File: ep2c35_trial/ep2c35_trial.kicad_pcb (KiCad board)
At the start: 4 copper layers, 50.3 x 39 mm, 5 parts, among them U1 EP2C5F484

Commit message: EP2C35 trial. WIP.
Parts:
- added J1: Conn_02x21_Odd_Even, Connector_PinHeader_1.27mm:PinHeader_2x21_P1.27mm_Horizontal, F.Cu at (143.2, 101.7)
- added J2: Conn_02x21_Odd_Even, Connector_PinHeader_1.27mm:PinHeader_2x21_P1.27mm_Horizontal, F.Cu at (171.2, 101.7)
- added J3: 3M_8540-4500PL, logic_analyzer:3M_8540-4500PL, F.Cu at (111.5, 100.2)
- added R11: 100, Resistor_SMD:R_0402_1005Metric, B.Cu at (154.5, 83.0)
- added R12: 100, Resistor_SMD:R_0402_1005Metric, B.Cu at (154.5, 84.0)
- added R13: 100, Resistor_SMD:R_0402_1005Metric, B.Cu at (154.5, 85.0)
- added R14: 100, Resistor_SMD:R_0402_1005Metric, B.Cu at (154.5, 86.0)
- added R15: 100, Resistor_SMD:R_0402_1005Metric, B.Cu at (154.5, 87.0)
- added R16: 100, Resistor_SMD:R_0402_1005Metric, B.Cu at (154.5, 88.0)
- added R17: 100, Resistor_SMD:R_0402_1005Metric, B.Cu at (154.5, 89.0)
- added R18: 100, Resistor_SMD:R_0402_1005Metric, B.Cu at (154.5, 90.0)
- added R19: 100, Resistor_SMD:R_0402_1005Metric, B.Cu at (152.2, 90.2)
- added R20: 100, Resistor_SMD:R_0402_1005Metric, B.Cu at (154.5, 82.0)
- added R21: 100, Resistor_SMD:R_0402_1005Metric, B.Cu at (134.5, 90.0)
- added R22: 100, Resistor_SMD:R_0402_1005Metric, B.Cu at (134.5, 89.0)
- added R23: 100, Resistor_SMD:R_0402_1005Metric, B.Cu at (134.5, 88.0)
- added R24: 100, Resistor_SMD:R_0402_1005Metric, B.Cu at (134.5, 87.0)
- added R25: 100, Resistor_SMD:R_0402_1005Metric, B.Cu at (134.5, 86.0)
- added R26: 100, Resistor_SMD:R_0402_1005Metric, B.Cu at (134.5, 85.0)
- added R27: 100, Resistor_SMD:R_0402_1005Metric, B.Cu at (134.5, 84.0)
- added R28: 100, Resistor_SMD:R_0402_1005Metric, B.Cu at (134.5, 83.0)
- added R29: 100, Resistor_SMD:R_0402_1005Metric, B.Cu at (136.7, 90.2)
- added R30: 100, Resistor_SMD:R_0402_1005Metric, B.Cu at (134.5, 82.0)
- added U2: XC6SLX16-FTG256, Package_BGA:Xilinx_FTG256, F.Cu at (173.2, 69.6)
- added U3: FT600Q-B-T, logic_analyzer:QFN-56-1EP_7x7mm_P0.4mm_FT600Q, F.Cu at (144.4, 60.8)
- moved C1 0.05 mm to (149.0, 75.5)
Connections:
- U1 pad A10: unconnected-(U1-PadA10) -> /FT_WR_N
- U1 pad A11: unconnected-(U1-PadA11) -> /FT_OE_N
- U1 pad A2: +2V5 -> +3.3V
- U1 pad A21: +2V5 -> +3.3V
- U1 pad A3: unconnected-(U1-PadA3) -> /FT_DATA7
- U1 pad A4: unconnected-(U1-PadA4) -> /FT_DATA8
- U1 pad A5: unconnected-(U1-PadA5) -> /FT_DATA10
- U1 pad A6: unconnected-(U1-PadA6) -> /FT_DATA12
- U1 pad A7: unconnected-(U1-PadA7) -> /FT_DATA14
- U1 pad A8: unconnected-(U1-PadA8) -> /FT_BE0
- U1 pad A9: unconnected-(U1-PadA9) -> /FT_TXE_N
- U1 pad B1: +2V5 -> +3.3V
- U1 pad B10: unconnected-(U1-PadB10) -> /FT_RD_N
- U1 pad B11: unconnected-(U1-PadB11) -> /FT_RESET_N
- U1 pad B22: +2V5 -> +3.3V
- U1 pad B3: unconnected-(U1-PadB3) -> /FT_CLK
- U1 pad B4: unconnected-(U1-PadB4) -> /FT_DATA9
- U1 pad B5: unconnected-(U1-PadB5) -> /FT_DATA11
- U1 pad B6: unconnected-(U1-PadB6) -> /FT_DATA13
- U1 pad B7: unconnected-(U1-PadB7) -> /FT_DATA15
- U1 pad B8: unconnected-(U1-PadB8) -> /FT_BE1
- U1 pad B9: unconnected-(U1-PadB9) -> /FT_RXF_N
- U1 pad C1: unconnected-(U1-PadC1) -> /FT_DATA5
- U1 pad C10: unconnected-(U1-PadC10) -> /FT_GPIO1
- U1 pad C11: +2V5 -> +3.3V
- U1 pad C12: +2V5 -> +3.3V
- U1 pad C2: unconnected-(U1-PadC2) -> /FT_DATA6
- U1 pad C6: +2V5 -> +3.3V
- U1 pad C9: unconnected-(U1-PadC9) -> /FT_WAKEUP_N
- U1 pad D1: unconnected-(U1-PadD1) -> /FT_DATA3
- U1 pad D17: +2V5 -> +3.3V
- U1 pad D2: unconnected-(U1-PadD2) -> /FT_DATA4
- U1 pad D9: unconnected-(U1-PadD9) -> /FT_GPIO0
- U1 pad E1: unconnected-(U1-PadE1) -> /FT_DATA1
- U1 pad E10: +2V5 -> +3.3V
- U1 pad E13: +2V5 -> +3.3V
- U1 pad E2: unconnected-(U1-PadE2) -> /FT_DATA2
- U1 pad F2: unconnected-(U1-PadF2) -> /FT_DATA0
- U1 pad G14: +2V5 -> +3.3V
- U1 pad G19: +2V5 -> +3.3V
- U1 pad G9: +2V5 -> +3.3V
- U1 pad J16: +2V5 -> +3.3V
- U1 pad J7: +2V5 -> +3.3V
- U1 pad L20: +2V5 -> +3.3V
- U1 pad L3: +2V5 -> +3.3V
- U1 pad M1: unconnected-(U1-PadM1) -> /LVDS_RX_CLK0_P
- U1 pad M2: unconnected-(U1-PadM2) -> /LVDS_RX_CLK0_N
- U1 pad M21: unconnected-(U1-PadM21) -> /LVDS_RX_CLK1_N
- U1 pad M22: unconnected-(U1-PadM22) -> GNDD
- U1 pad M5: unconnected-(U1-PadM5) -> Net-(U1-PadM5)
- U1 pad M6: unconnected-(U1-PadM6) -> Net-(U1-PadM5)
- U1 pad M7: unconnected-(U1-PadM7) -> Net-(U1-PadM7)
- U1 pad M8: unconnected-(U1-PadM8) -> Net-(U1-PadM7)
- U1 pad N1: unconnected-(U1-PadN1) -> /LVDS_RX_DATA0_0_P
- U1 pad N2: unconnected-(U1-PadN2) -> /LVDS_RX_DATA0_0_N
- U1 pad N21: unconnected-(U1-PadN21) -> /LVDS_RX_DATA1_7_N
- U1 pad N22: unconnected-(U1-PadN22) -> /LVDS_RX_DATA1_7_P
- U1 pad N3: unconnected-(U1-PadN3) -> Net-(U1-PadN3)
- U1 pad N4: unconnected-(U1-PadN4) -> Net-(U1-PadN3)
- U1 pad N5: unconnected-(U1-PadN5) -> Net-(U1-PadN5)
- U1 pad N6: unconnected-(U1-PadN6) -> Net-(U1-PadN5)
- U1 pad P1: unconnected-(U1-PadP1) -> /LVDS_RX_DATA0_1_P
- U1 pad P2: unconnected-(U1-PadP2) -> /LVDS_RX_DATA0_1_N
- U1 pad P21: unconnected-(U1-PadP21) -> /LVDS_RX_DATA1_6_N
- U1 pad P22: unconnected-(U1-PadP22) -> /LVDS_RX_DATA1_6_P
- U1 pad P4: unconnected-(U1-PadP4) -> Net-(U1-PadP4)
- U1 pad P5: unconnected-(U1-PadP5) -> Net-(U1-PadP5)
- U1 pad P6: unconnected-(U1-PadP6) -> Net-(U1-PadP5)
- U1 pad R1: unconnected-(U1-PadR1) -> /LVDS_RX_DATA0_2_P
- U1 pad R2: unconnected-(U1-PadR2) -> /LVDS_RX_DATA0_2_N
- U1 pad R21: unconnected-(U1-PadR21) -> /LVDS_RX_DATA1_5_N
- U1 pad R22: unconnected-(U1-PadR22) -> /LVDS_RX_DATA1_5_P
- U1 pad R4: unconnected-(U1-PadR4) -> Net-(U1-PadP4)
- U1 pad R5: unconnected-(U1-PadR5) -> Net-(U1-PadR5)
- U1 pad R6: unconnected-(U1-PadR6) -> Net-(U1-PadR5)
- U1 pad R7: unconnected-(U1-PadR7) -> Net-(U1-PadR7)
- U1 pad R8: unconnected-(U1-PadR8) -> Net-(U1-PadR7)
- U1 pad T1: unconnected-(U1-PadT1) -> /LVDS_RX_DATA0_3_P
- U1 pad T2: unconnected-(U1-PadT2) -> /LVDS_RX_DATA0_3_N
- U1 pad T21: unconnected-(U1-PadT21) -> /LVDS_RX_DATA1_4_N
- U1 pad T22: unconnected-(U1-PadT22) -> /LVDS_RX_DATA1_4_P
- U1 pad T5: unconnected-(U1-PadT5) -> Net-(U1-PadT5)
- U1 pad T6: unconnected-(U1-PadT6) -> Net-(U1-PadT5)
- U1 pad U1: unconnected-(U1-PadU1) -> /LVDS_RX_DATA0_4_P
- U1 pad U2: unconnected-(U1-PadU2) -> /LVDS_RX_DATA0_4_N
- U1 pad U21: unconnected-(U1-PadU21) -> /LVDS_RX_DATA1_3_N
- U1 pad U22: unconnected-(U1-PadU22) -> /LVDS_RX_DATA1_3_P
- U1 pad V1: unconnected-(U1-PadV1) -> /LVDS_RX_DATA0_5_P
- U1 pad V2: unconnected-(U1-PadV2) -> /LVDS_RX_DATA0_5_N
- U1 pad V21: unconnected-(U1-PadV21) -> /LVDS_RX_DATA1_2_N
- U1 pad V22: unconnected-(U1-PadV22) -> /LVDS_RX_DATA1_2_P
- U1 pad W1: unconnected-(U1-PadW1) -> /LVDS_RX_DATA0_6_P
- U1 pad W2: unconnected-(U1-PadW2) -> /LVDS_RX_DATA0_6_N
- U1 pad W21: unconnected-(U1-PadW21) -> /LVDS_RX_DATA1_1_N
- U1 pad W22: unconnected-(U1-PadW22) -> /LVDS_RX_DATA1_1_P
- U1 pad W3: unconnected-(U1-PadW3) -> Net-(U1-PadW3)
- U1 pad W4: unconnected-(U1-PadW4) -> Net-(U1-PadW3)
- U1 pad Y1: unconnected-(U1-PadY1) -> /LVDS_RX_DATA0_7_P
- U1 pad Y19: unconnected-(U1-PadY19) -> /LVDS_RX_FCLK1_N
- U1 pad Y2: unconnected-(U1-PadY2) -> /LVDS_RX_DATA0_7_N
- U1 pad Y20: unconnected-(U1-PadY20) -> /LVDS_RX_FCLK1_P
- U1 pad Y21: unconnected-(U1-PadY21) -> /LVDS_RX_DATA1_0_N
- U1 pad Y22: unconnected-(U1-PadY22) -> /LVDS_RX_DATA1_0_P
- U1 pad Y3: unconnected-(U1-PadY3) -> /LVDS_RX_FCLK0_P
- U1 pad Y4: unconnected-(U1-PadY4) -> /LVDS_RX_FCLK0_N
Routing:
- net /LVDS_RX_DATA0_2_N: track 0.00 -> 37.8 mm, vias 0 -> 1
- net /LVDS_RX_DATA0_2_P: track 0.00 -> 37.2 mm, vias 0 -> 1
- net /LVDS_RX_DATA0_3_N: track 0.00 -> 36.9 mm, vias 0 -> 1
- net /LVDS_RX_DATA0_3_P: track 0.00 -> 36.3 mm, vias 0 -> 1
- net /LVDS_RX_DATA0_4_N: track 0.00 -> 36.1 mm, vias 0 -> 1
- net /LVDS_RX_DATA0_4_P: track 0.00 -> 35.0 mm, vias 0 -> 1
- net /LVDS_RX_DATA1_6_N: track 0.00 -> 33.6 mm, vias 0 -> 1
- net /LVDS_RX_DATA0_1_N: track 0.00 -> 33.5 mm, vias 0 -> 1
- net /LVDS_RX_DATA1_7_N: track 0.00 -> 33.5 mm, vias 0 -> 1
- net /LVDS_RX_DATA1_5_N: track 0.00 -> 33.5 mm, vias 0 -> 1
- net /LVDS_RX_DATA0_0_N: track 0.00 -> 33.4 mm, vias 0 -> 1
- net /LVDS_RX_DATA1_4_N: track 0.00 -> 33.4 mm, vias 0 -> 1
- net /LVDS_RX_DATA1_3_N: track 0.00 -> 33.3 mm, vias 0 -> 1
- net /LVDS_RX_DATA1_2_N: track 0.00 -> 33.3 mm, vias 0 -> 1
- net /LVDS_RX_DATA1_0_N: track 0.00 -> 33.3 mm, vias 0 -> 1
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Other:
- board size 50.3 x 39 mm -> 81.1 x 57.6 mm

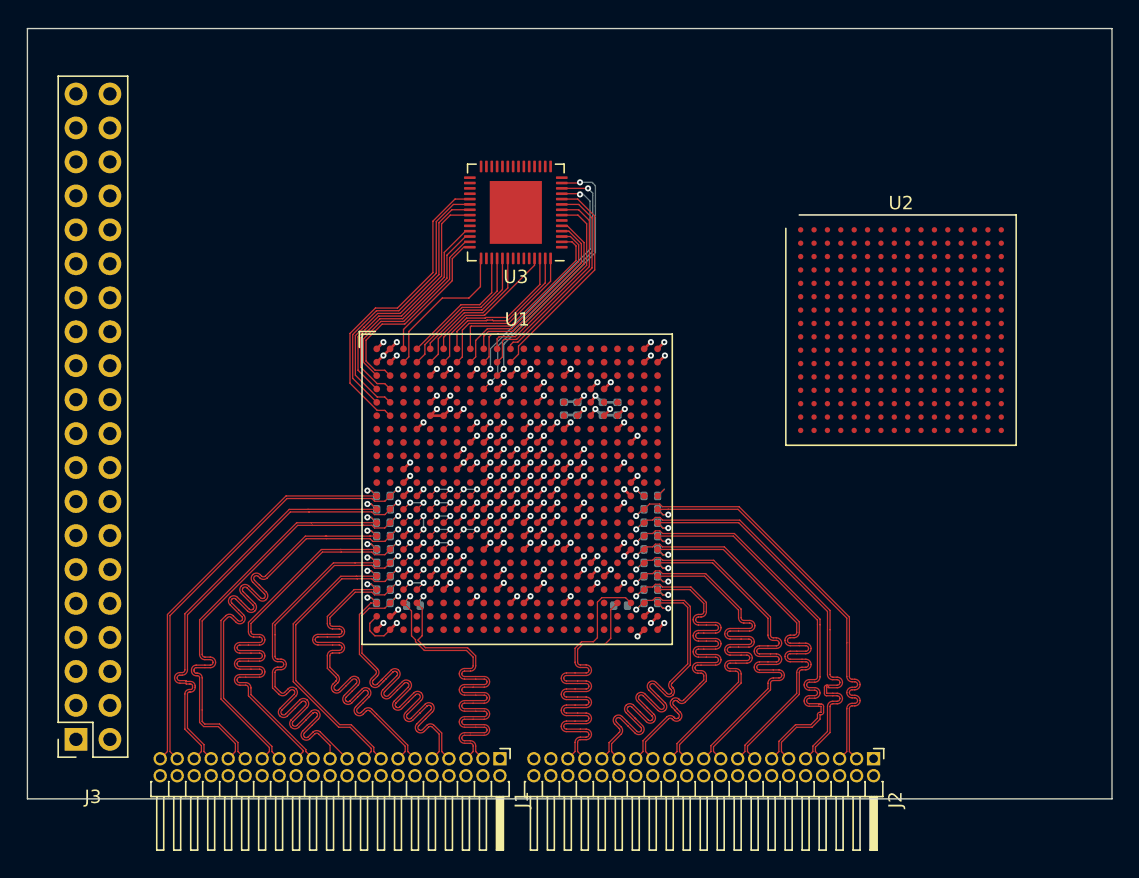
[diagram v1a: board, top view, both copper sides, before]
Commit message: Wire up FTDI FT600Q.
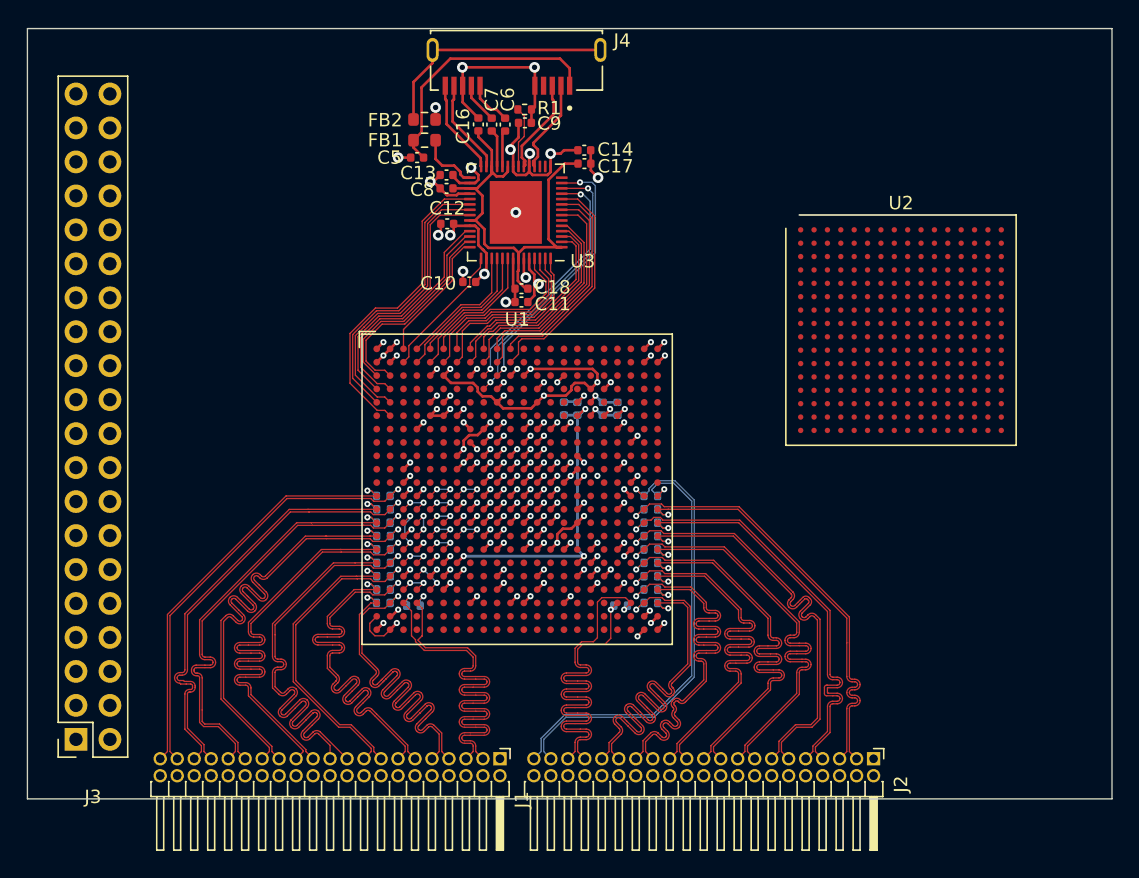
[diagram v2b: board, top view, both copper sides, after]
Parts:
- added C10: 100n, Capacitor_SMD:C_0402_1005Metric, F.Cu at (140.9, 66.0)
- added C11: 100n, Capacitor_SMD:C_0402_1005Metric, F.Cu at (144.8, 67.5)
- added C12: 100n, Capacitor_SMD:C_0402_1005Metric, F.Cu at (139.3, 61.6)
- added C13: 100n, Capacitor_SMD:C_0402_1005Metric, F.Cu at (139.2, 58.0)
- added C14: 100n, Capacitor_SMD:C_0402_1005Metric, F.Cu at (149.5, 56.1)
- added C16: 100n, Capacitor_SMD:C_0402_1005Metric, F.Cu at (141.6, 54.2)
- added C17: 100n, Capacitor_SMD:C_0402_1005Metric, F.Cu at (149.5, 57.1)
- added C18: 100n, Capacitor_SMD:C_0402_1005Metric, F.Cu at (144.8, 66.5)
- added C5: 0.1u, Capacitor_SMD:C_0402_1005Metric, F.Cu at (137.0, 56.7)
- added C6: 0.1u, Capacitor_SMD:C_0402_1005Metric, F.Cu at (143.6, 54.2)
- added C7: 0.1u, Capacitor_SMD:C_0402_1005Metric, F.Cu at (142.6, 54.2)
- added C8: 4.7u, Capacitor_SMD:C_0402_1005Metric, F.Cu at (139.2, 59.0)
- added C9: 100n, Capacitor_SMD:C_0402_1005Metric, F.Cu at (145.1, 54.1)
- added FB1: BLM18PG221SN1D, Resistor_SMD:R_0603_1608Metric, F.Cu at (137.6, 55.4)
- added FB2: BLM18PG221SN1D, Resistor_SMD:R_0603_1608Metric, F.Cu at (137.6, 53.9)
- added J4: USB3_B_Micro_Amphenol_GSB343K331HR, Amphenol_GSB343K331HR:AMPHENOL_GSB343K331HR, F.Cu at (144.4, 48.6)
- added R1: 1.6k/1%, Resistor_SMD:R_0402_1005Metric, F.Cu at (145.1, 53.1)
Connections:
- J2 pad 41: GNDD -> /LVDS_RX_CLK1_P
- R20 pad 2: GNDD -> /LVDS_RX_CLK1_P
- U1 pad M22: GNDD -> /LVDS_RX_CLK1_P
- U1 pad P3: unconnected-(U1-PadP3) -> Net-(U1-PadT3)
- U1 pad T3: unconnected-(U1-PadT3) -> Net-(U1-PadT3)
- U1 pad U3: unconnected-(U1-PadU3) -> Net-(U1-PadU4)
- U1 pad U4: unconnected-(U1-PadU4) -> Net-(U1-PadU4)
- U1 pad V4: unconnected-(U1-PadV4) -> Net-(U1-PadV4)
- U1 pad V7: GNDA -> GNDD
- U1 pad W5: unconnected-(U1-PadW5) -> Net-(U1-PadV4)
- U3 pad 1: unconnected-(U3-Pad1) -> +1V0
- U3 pad 15: unconnected-(U3-Pad15) -> +3.3V
- U3 pad 18: unconnected-(U3-Pad18) -> /USB_D_N
- U3 pad 19: unconnected-(U3-Pad19) -> +3.3V
- U3 pad 20: unconnected-(U3-Pad20) -> /USB_D_P
- U3 pad 21: unconnected-(U3-Pad21) -> /USB_RREF
- U3 pad 22: unconnected-(U3-Pad22) -> +3.3V
- U3 pad 23: unconnected-(U3-Pad23) -> +1V0
- U3 pad 24: unconnected-(U3-Pad24) -> /USB_SSTX_N
- U3 pad 25: unconnected-(U3-Pad25) -> /USB_SSTX_P
- U3 pad 26: unconnected-(U3-Pad26) -> +1V0
- U3 pad 27: unconnected-(U3-Pad27) -> /USB_SSRX_N
- U3 pad 28: unconnected-(U3-Pad28) -> /USB_SSRX_P
- U3 pad 29: unconnected-(U3-Pad29) -> /VBUS
- U3 pad 30: unconnected-(U3-Pad30) -> +3.3V
- U3 pad 31: unconnected-(U3-Pad31) -> +1V0
- U3 pad 32: unconnected-(U3-Pad32) -> GNDD
- U3 pad 37: unconnected-(U3-Pad37) -> +1V0
- U3 pad 38: unconnected-(U3-Pad38) -> +3.3V
- U3 pad 44: unconnected-(U3-Pad44) -> +3.3V
- U3 pad 49: unconnected-(U3-Pad49) -> GNDD
- U3 pad 50: unconnected-(U3-Pad50) -> +1V0
- U3 pad 51: unconnected-(U3-Pad51) -> GNDD
- U3 pad 52: unconnected-(U3-Pad52) -> +3.3V
- U3 pad 57: unconnected-(U3-Pad57) -> GNDD
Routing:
- net +3.3V: track 12.7 -> 70.0 mm, vias 17 -> 25
- net /LVDS_RX_CLK1_P: track 0.00 -> 33.8 mm, vias 0 -> 1
- net +1V0: track 0.00 -> 33.5 mm
- net /LVDS_RX_CLK1_N: track 1.59 -> 34.6 mm
- net GNDD: track 60.6 -> 89.6 mm, vias 76 -> 88
- net +1V2A: track 4.55 -> 24.6 mm
- net /VBUS_RAW: track 0.00 -> 19.4 mm
- net /USB_SHIELD: track 0.00 -> 18.3 mm
- net /USB_D_P: track 0.00 -> 7.21 mm
- net /USB_D_N: track 0.00 -> 7.20 mm
- net /USB_SSRX_N: track 0.00 -> 7.15 mm
- net /USB_SSRX_P: track 0.00 -> 7.15 mm
- net /VBUS: track 0.00 -> 4.65 mm
- net /USB_RREF: track 0.00 -> 4.64 mm
- net Net-(U1-PadT3): track 0.00 -> 3.75 mm, vias 0 -> 2
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- added copper zone on In2.Cu, net +2V5
- added copper zone on In2.Cu, net +3.3V

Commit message: Before switching to hierarchical sheets.
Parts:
- added C15: 100n, Capacitor_SMD:C_0402_1005Metric, F.Cu at (125.5, 61.8)
- added J5: Conn_02x05_Odd_Even, Connector_PinHeader_2.54mm:PinHeader_2x05_P2.54mm_Vertical, F.Cu at (129.5, 49.3)
- added R2: 10K, Resistor_SMD:R_0402_1005Metric, B.Cu at (136.5, 80.8)
- added R3: 10K, Resistor_SMD:R_0402_1005Metric, F.Cu at (120.2, 58.4)
- added R4: 10K, Resistor_SMD:R_0402_1005Metric, F.Cu at (130.7, 57.2)
- added R5: 10K, Resistor_SMD:R_0402_1005Metric, B.Cu at (152.8, 82.5)
- added R6: 10K, Resistor_SMD:R_0402_1005Metric, B.Cu at (150.8, 82.5)
- added TP1: TestPoint, TestPoint:TestPoint_Pad_D1.0mm, F.Cu at (134.8, 66.7)
- added U4: W25Q16JVSNIQ, Package_SO:SOIC-8_5.23x5.23mm_P1.27mm, F.Cu at (125.5, 58.4)
- moved J3 69.4 mm to (180.9, 100.2)
- moved U2 56.0 mm to (117.3, 72.8)
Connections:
- net Net-(U1-PadM5) renamed /LVDS26
- net Net-(U1-PadM7) renamed /LVDS23
- net Net-(U1-PadN3) renamed /LVDS20
- net Net-(U1-PadN5) renamed /LVDS22
- net Net-(U1-PadP4) renamed /LVDS12
- net Net-(U1-PadP5) renamed /LVDS17
- net Net-(U1-PadR5) renamed /LVDS10
- net Net-(U1-PadR7) renamed /LVDS18
- net Net-(U1-PadT5) renamed /LVDS7
- net Net-(U1-PadW3) renamed /LVDS2
- J3 pad 1: unconnected-(J3-Pad1) -> +5V
- J3 pad 10: unconnected-(J3-Pad10) -> GNDD
- J3 pad 11: unconnected-(J3-Pad11) -> /POD_D13
- J3 pad 12: unconnected-(J3-Pad12) -> GNDD
- J3 pad 13: unconnected-(J3-Pad13) -> /POD_D12
- J3 pad 14: unconnected-(J3-Pad14) -> GNDD
- J3 pad 15: unconnected-(J3-Pad15) -> /POD_D11
- J3 pad 16: unconnected-(J3-Pad16) -> GNDD
- J3 pad 17: unconnected-(J3-Pad17) -> /POD_D10
- J3 pad 18: unconnected-(J3-Pad18) -> GNDD
- J3 pad 19: unconnected-(J3-Pad19) -> /POD_D9
- J3 pad 2: unconnected-(J3-Pad2) -> GNDD
- J3 pad 20: unconnected-(J3-Pad20) -> GNDD
- J3 pad 21: unconnected-(J3-Pad21) -> /POD_D8
- J3 pad 22: unconnected-(J3-Pad22) -> GNDD
- J3 pad 23: unconnected-(J3-Pad23) -> /POD_D7
- J3 pad 24: unconnected-(J3-Pad24) -> GNDD
- J3 pad 25: unconnected-(J3-Pad25) -> /POD_D6
- J3 pad 26: unconnected-(J3-Pad26) -> GNDD
- J3 pad 27: unconnected-(J3-Pad27) -> /POD_D5
- J3 pad 28: unconnected-(J3-Pad28) -> GNDD
- J3 pad 29: unconnected-(J3-Pad29) -> /POD_D4
- J3 pad 3: unconnected-(J3-Pad3) -> /POD_CLK
- J3 pad 30: unconnected-(J3-Pad30) -> GNDD
- J3 pad 31: unconnected-(J3-Pad31) -> /POD_D3
- J3 pad 32: unconnected-(J3-Pad32) -> GNDD
- J3 pad 33: unconnected-(J3-Pad33) -> /POD_D2
- J3 pad 34: unconnected-(J3-Pad34) -> GNDD
- J3 pad 35: unconnected-(J3-Pad35) -> /POD_D1
- J3 pad 36: unconnected-(J3-Pad36) -> GNDD
- J3 pad 37: unconnected-(J3-Pad37) -> /POD_D0
- J3 pad 38: unconnected-(J3-Pad38) -> GNDD
- J3 pad 39: unconnected-(J3-Pad39) -> +5V
- J3 pad 4: unconnected-(J3-Pad4) -> GNDD
- J3 pad 40: unconnected-(J3-Pad40) -> GNDD
- J3 pad 6: unconnected-(J3-Pad6) -> GNDD
- J3 pad 7: unconnected-(J3-Pad7) -> /POD_D15
- J3 pad 8: unconnected-(J3-Pad8) -> GNDD
- J3 pad 9: unconnected-(J3-Pad9) -> /POD_D14
- U1 pad C3: unconnected-(U1-PadC3) -> /SPI_nCS
- U1 pad C4: unconnected-(U1-PadC4) -> /SPI_ADS
- U1 pad D3: unconnected-(U1-PadD3) -> /CRC_ERROR
- U1 pad K1: unconnected-(U1-PadK1) -> GNDD
- U1 pad K2: unconnected-(U1-PadK2) -> /TCK
- U1 pad K4: unconnected-(U1-PadK4) -> /SPI_DATA0
- U1 pad K5: unconnected-(U1-PadK5) -> /TDI
- U1 pad K6: unconnected-(U1-PadK6) -> /TMS
- U1 pad L4: unconnected-(U1-PadL4) -> Net-(U1-PadL4)
- U1 pad L5: unconnected-(U1-PadL5) -> /TDO
- U1 pad L6: unconnected-(U1-PadL6) -> /SPI_DCLK
- U1 pad M17: unconnected-(U1-PadM17) -> GNDD
- U1 pad N17: unconnected-(U1-PadN17) -> GNDD
- U1 pad N18: unconnected-(U1-PadN18) -> /CONF_DONE
- U1 pad N20: unconnected-(U1-PadN20) -> /nSTATUS
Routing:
- net /SPI_DATA0: track 0.00 -> 47.6 mm, vias 0 -> 2
- net /TDI: track 0.00 -> 46.1 mm, vias 0 -> 2
- net /TMS: track 0.00 -> 43.4 mm, vias 0 -> 1
- net /TDO: track 0.00 -> 39.4 mm, vias 0 -> 2
- net /TCK: track 0.00 -> 34.0 mm, vias 0 -> 1
- net /SPI_nCS: track 0.00 -> 32.2 mm, vias 0 -> 2
- net /SPI_DCLK: track 0.00 -> 29.9 mm, vias 0 -> 2
- net /SPI_ADS: track 0.00 -> 20.5 mm, vias 0 -> 2
- net +3.3V: track 70.0 -> 87.8 mm, vias 25 -> 26
- net /CRC_ERROR: track 0.00 -> 10.1 mm, vias 0 -> 2
- net GNDD: track 89.6 -> 95.5 mm, vias 88 -> 90
- net +2V5: track 17.7 -> 20.3 mm
- net /SPI_nWP: track 0.00 -> 1.77 mm
- net /nSTATUS: track 0.00 -> 1.65 mm, vias 0 -> 1
- net /SPI_nRESET: track 0.00 -> 1.64 mm
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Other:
- board size 81.1 x 57.6 mm -> 78 x 57.6 mm
